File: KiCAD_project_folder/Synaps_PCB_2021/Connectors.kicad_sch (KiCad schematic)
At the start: 0 parts

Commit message: Redid schematic, fixed wrong setup
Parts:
- added J2: Conn_01x20_MountingPin, symbol Connector_Generic_MountingPin:Conn_01x20_MountingPin
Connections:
- new net CAN_BUS_CLK: J2.4 (Pin_4)
- new net CAN_BUS_OFF_ON: J2.5 (Pin_5)
- new net CAN_BUS_RX: J2.2 (Pin_2)
- new net CAN_BUS_TX: J2.3 (Pin_3)
- new net GNDREF: J2.1 (Pin_1), J2.14 (Pin_14), J2.17 (Pin_17), J2.20 (Pin_20), J2.6 (Pin_6), J2.9 (Pin_9), J2.MP (MountPin)
- new net GPIO11: J2.15 (Pin_15), J2.16 (Pin_16)
- new net JTAG_MTDCK: J2.13 (Pin_13)
- new net JTAG_MTDI: J2.11 (Pin_11)
- new net JTAG_MTDO: J2.12 (Pin_12)
- new net JTAG_MTDS: J2.10 (Pin_10)
- new net UART_RX: J2.18 (Pin_18)
- new net UART_TX: J2.19 (Pin_19)
- no-connect marks 0 -> 2
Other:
- note added: "CAN BUS INTERFACE"
- note added: "JTAG_INTERFACE"
- note added: "UART INTERFACE"

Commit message: Updated pcb editor with the new components imported
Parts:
- J2: footprint (none) -> Connector_PinHeader_2.00mm:PinHeader_1x20_P2.00mm_Vertical
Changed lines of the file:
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@@
       (effects (font (size 1.27 1.27)) (justify left))
     )
-    (property "Footprint" "" (id 2) (at 194.31 58.42 0)
+    (property "Footprint" "Connector_PinHeader_2.00mm:PinHeader_1x20_P2.00mm_Vertical" (id 2) (at 194.31 58.42 0)
       (effects (font (size 1.27 1.27)) hide)
     )

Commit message: Update schematic sheets and creates image to allow the board setup to be shared
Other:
- company: (none) -> Club SynapsÉTS
- title: (none) -> Misca PCB
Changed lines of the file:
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@@
 (kicad_sch (version 20211123) (generator eeschema)
   (paper "A4")
+  (title_block
+    (title "Misca PCB")
+    (date "2022-06-17")
+    (rev "A2")
+    (company "Club SynapsÉTS")
+    (comment 1 "Auteur : Jacques Veneziano")
+  )
   (no_connect (at 189.23 50.8))
   (no_connect (at 189.23 53.34))

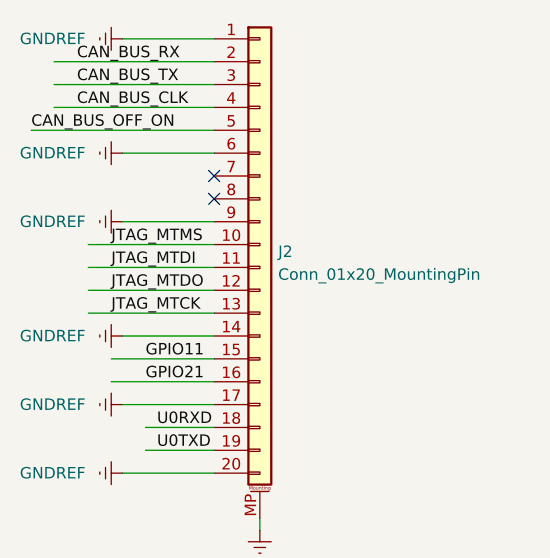
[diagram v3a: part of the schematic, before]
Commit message: Updated BOM and power circuit has to be redone because of missing parts
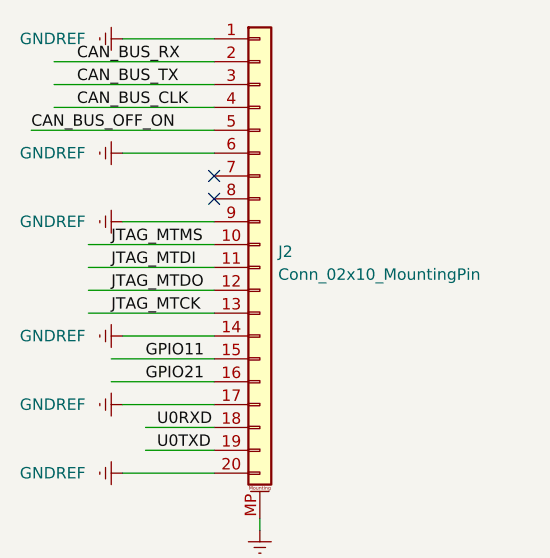
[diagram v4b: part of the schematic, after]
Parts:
- J2: value Conn_01x20_MountingPin -> Conn_02x10_MountingPin; footprint Connector_PinHeader_2.00mm:PinHeader_1x20_P2.00mm_Vertical -> Connector_PinHeader_2.54mm:PinHeader_2x10_P2.54mm_Vertical_SMD; MPN (none) -> 3020-20-0300-00; Supplier Link (none) -> https://www.digikey.ca/en/products/detail/cnc-tech/3020-20-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
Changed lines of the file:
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@@
       (effects (font (size 1.27 1.27)) (justify left))
     )
-    (property "Value" "Conn_01x20_MountingPin" (id 1) (at 196.342 61.7478 0)
+    (property "Value" "Conn_02x10_MountingPin" (id 1) (at 196.342 61.7478 0)
       (effects (font (size 1.27 1.27)) (justify left))
     )
-    (property "Footprint" "Connector_PinHeader_2.00mm:PinHeader_1x20_P2.00mm_Vertical" (id 2) (at 194.31 58.42 0)
+    (property "Footprint" "Connector_PinHeader_2.54mm:PinHeader_2x10_P2.54mm_Vertical_SMD" (id 2) (at 194.31 58.42 0)
       (effects (font (size 1.27 1.27)) hide)
     )
-    (property "Datasheet" "~" (id 3) (at 194.31 58.42 0)
+    (property "Datasheet" "https://www.cnctech.us/pdfs/3020-XX-0300-00%20(9T).pdf" (id 3) (at 194.31 58.42 0)
       (effects (font (size 1.27 1.27)) hide)
     )
+    (property "MPN" "3020-20-0300-00" (id 4) (at 194.31 58.42 0)
+      (effects (font (size 1.27 1.27)) hide)
+    )
+    (property "Supplier Link" "https://www.digikey.ca/en/products/detail/cnc-tech/3020-20-0300-00/3441742" (id 5) (at 194.31 58.42 0)
+      (effects (font (size 1.27 1.27)) hide)
+    )

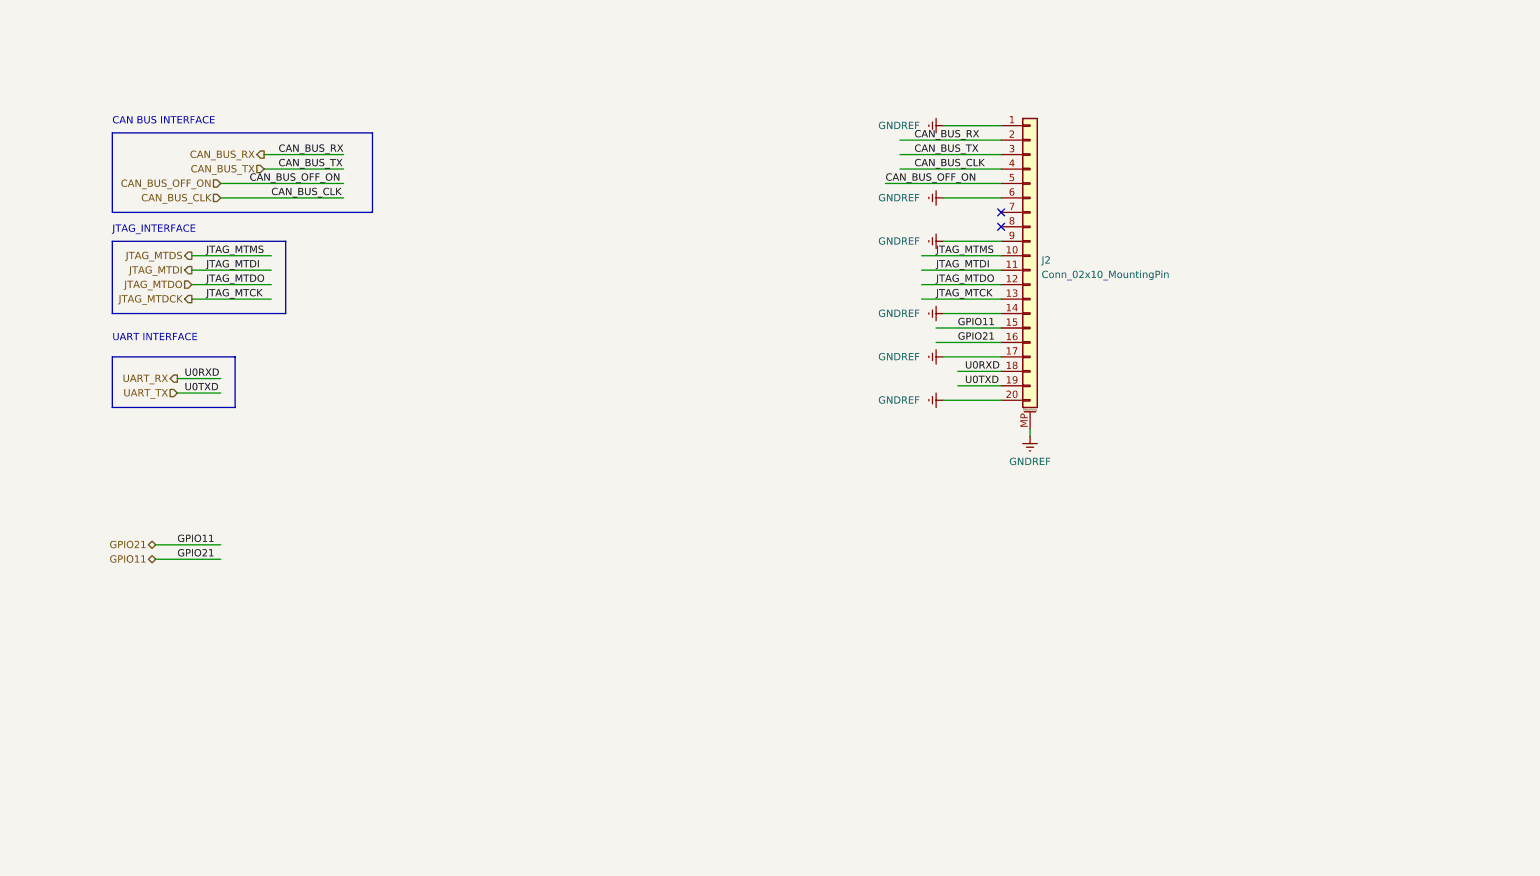
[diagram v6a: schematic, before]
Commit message: Transistionned board to ESP32S3, wip
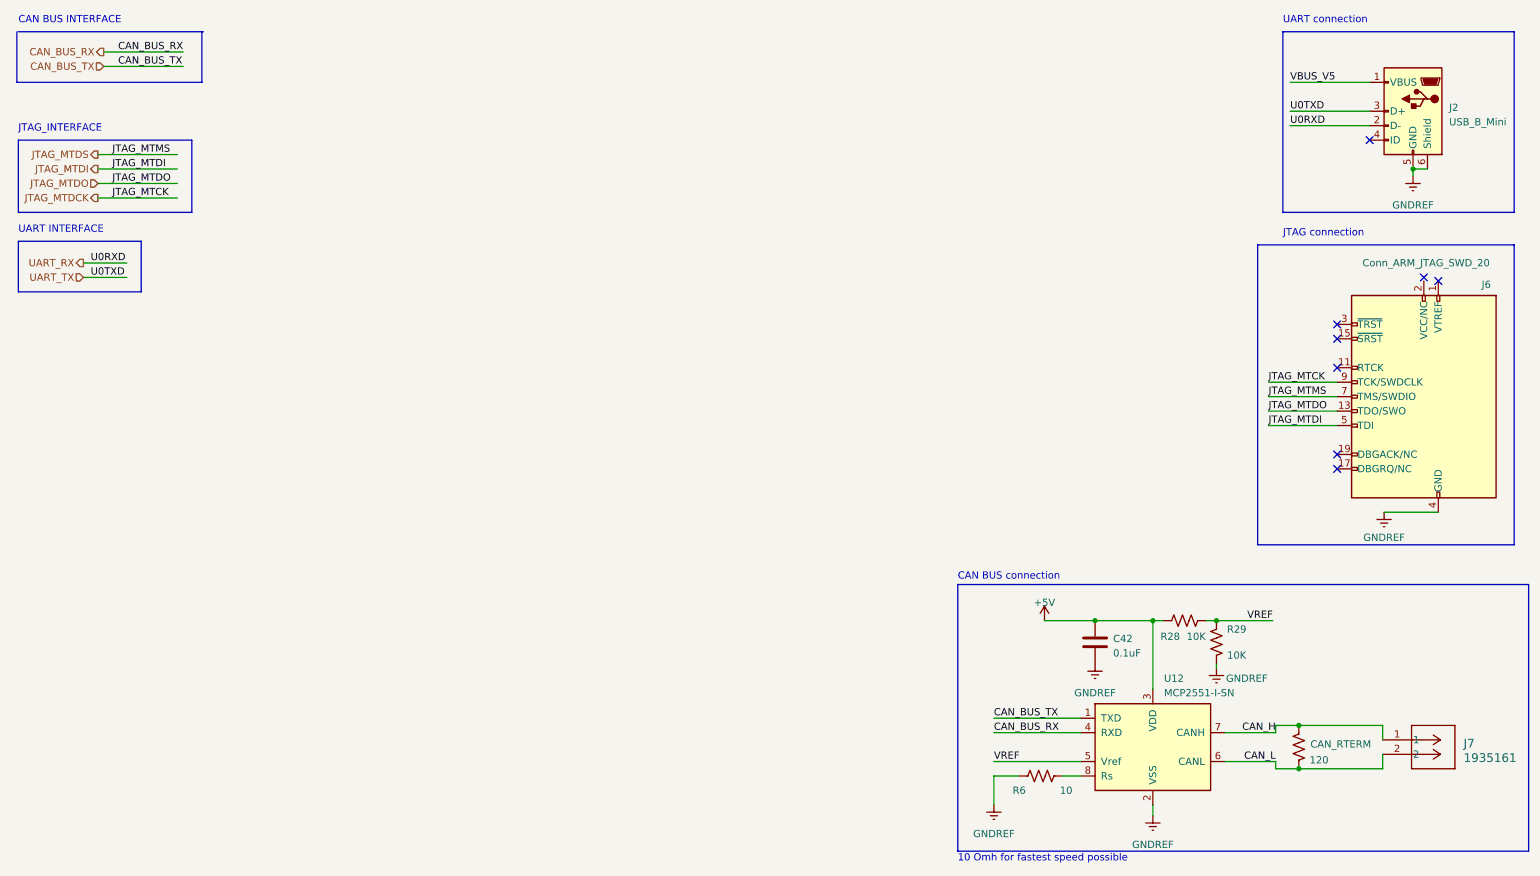
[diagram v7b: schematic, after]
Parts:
- removed J2: Conn_02x10_MountingPin, Connector_PinHeader_2.54mm:PinHeader_2x10_P2.54mm_Vertical_SMD, symbol Connector_Generic_MountingPin:Conn_01x20_MountingPin
- added C42: 0.1uF, symbol Device:C
- added CAN_RTERM: 120, symbol Device:R_US
- added J2: USB_B_Mini, symbol Connector:USB_B_Mini
- added J6: Conn_ARM_JTAG_SWD_20, symbol Connector:Conn_ARM_JTAG_SWD_20
- added J7: 1935161, CONN_1935161_PXC, symbol 1935161:1935161
- added R28, R29: 10K, symbol Device:R_US
- added R6: 10, symbol Device:R_US
- added U12: MCP2551-I-SN, Package_SO:SOIC-8_3.9x4.9mm_P1.27mm, symbol Interface_CAN_LIN:MCP2551-I-SN
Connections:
- net CAN_BUS_RX: now also U12.4 (RXD)
- net CAN_BUS_TX: now also U12.1 (TXD)
- net GNDREF: now also C42.2, J2.5 (GND), J2.6 (Shield), J6.10 (GND), J6.12 (GND), J6.14 (GND), J6.16 (GND), J6.18 (GND), J6.20 (GND), J6.4 (GND), J6.6 (GND), J6.8 (GND), R29.1, R6.1, U12.2 (VSS)
- net JTAG_MTDCK: now also J6.9 (TCK/SWDCLK)
- net JTAG_MTDI: now also J6.5 (TDI)
- net JTAG_MTDO: now also J6.13 (TDO/SWO)
- net JTAG_MTDS: now also J6.7 (TMS/SWDIO)
- net UART_RX: now also J2.2 (D-)
- net UART_TX: now also J2.3 (D+)
- new net: R6.2, U12.8 (Rs)
- new net +5V: C42.1, R28.2, U12.3 (VDD)
- new net CAN_H: CAN_RTERM.2, J7.1, U12.7 (CANH)
- new net CAN_L: CAN_RTERM.1, J7.2, U12.6 (CANL)
- new net VBUS_V5: J2.1 (VBUS)
- new net VREF: R28.1, R29.2, U12.5 (Vref)
- no-connect marks 2 -> 8
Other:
- note added: "10 Omh for fastest speed possible"
- note added: "CAN BUS connection"
- note added: "JTAG connection"
- note added: "UART connection"
